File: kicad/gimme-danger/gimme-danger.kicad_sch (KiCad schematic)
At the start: 67 parts, among them J3 Screw_Terminal_01x06, Q1 AO3400A, Q2 AO3400A, Q3 AO3400A, Q4 AO3400A, U1 ESP32-S3-WROOM-1, U11 DDTC143EUA, U2 TYPE-C-31-M-12, U3 TPD4E1U06DCKR, U4 DC-84, U5 SKRKAEE020, U7 SKRKAEE020, U8 TPS54302, U9 INA219AIDR

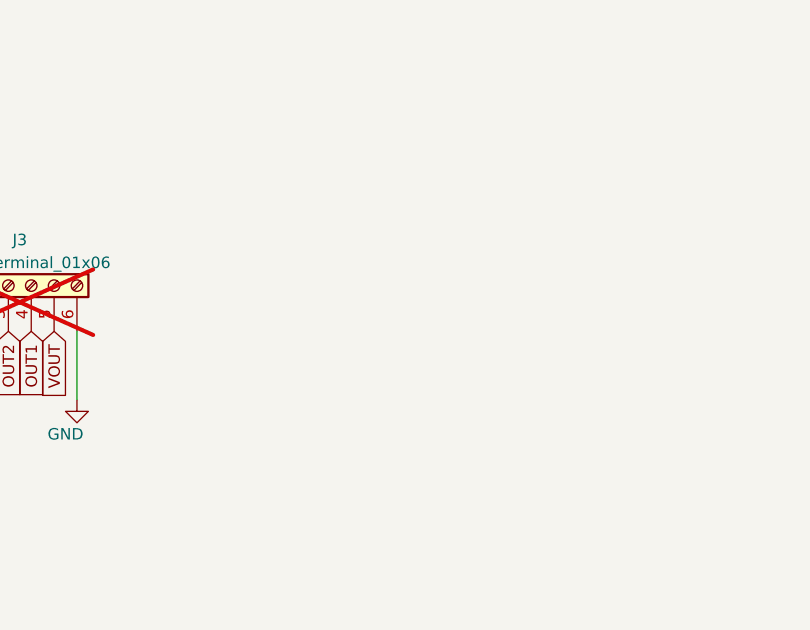
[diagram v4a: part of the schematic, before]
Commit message: Added mounting holes
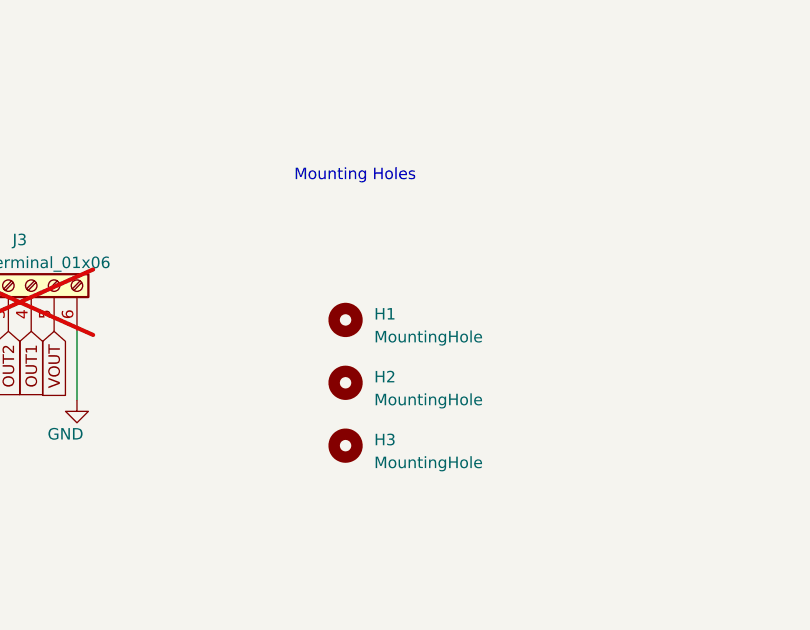
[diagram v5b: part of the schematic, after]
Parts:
- added H1, H2, H3: MountingHole, MountingHole:MountingHole_2.2mm_M2_Pad_Via, symbol Mechanical:MountingHole
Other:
- note added: "Mounting Holes"
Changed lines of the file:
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@@
+    (effects (font (size 1.27 1.27)) (justify left bottom))
+  )
+  (text "Mounting Holes" (at 119.38 220.345 0)
     (effects (font (size 1.27 1.27)) (justify left bottom))
   )
@@
     )
   )
+  (symbol (lib_id "Mechanical:MountingHole") (at 125.095 235.585 0) (unit 1)
+    (in_bom yes) (on_board yes) (dnp no) (fields_autoplaced)
+    (property "Reference" "H1" (at 128.27 234.95 0)
+      (effects (font (size 1.27 1.27)) (justify left))
+    )
+    (property "Value" "MountingHole" (at 128.27 237.49 0)
+      (effects (font (size 1.27 1.27)) (justify left))
+    )
+    (property "Footprint" "MountingHole:MountingHole_2.2mm_M2_Pad_Via" (at 125.095 235.585 0)
+      (effects (font (size 1.27 1.27)) hide)
+    )
+    (property "Datasheet" "~" (at 125.095 235.585 0)
+      (effects (font (size 1.27 1.27)) hide)
+    )
+    (instances
+      (project "gimme-danger"
+        (path "/1c42681d-64d0-4eab-a75f-10bf5c65177a"
+          (reference "H1") (unit 1)
+        )
+      )
+    )
+  )
   (symbol (lib_id "power:GND") (at 168.275 172.72 0) (unit 1)
     (in_bom yes) (on_board yes) (dnp no)
@@
     )
   )
+  (symbol (lib_id "Mechanical:MountingHole") (at 125.095 249.555 0) (unit 1)
+    (in_bom yes) (on_board yes) (dnp no) (fields_autoplaced)
+    (property "Reference" "H3" (at 128.27 248.92 0)
+      (effects (font (size 1.27 1.27)) (justify left))
+    )
+    (property "Value" "MountingHole" (at 128.27 251.46 0)
+      (effects (font (size 1.27 1.27)) (justify left))
+    )
+    (property "Footprint" "MountingHole:MountingHole_2.2mm_M2_Pad_Via" (at 125.095 249.555 0)
+      (effects (font (size 1.27 1.27)) hide)
+    )
+    (property "Datasheet" "~" (at 125.095 249.555 0)
+      (effects (font (size 1.27 1.27)) hide)
+    )
+    (instances
+      (project "gimme-danger"
+        (path "/1c42681d-64d0-4eab-a75f-10bf5c65177a"
+          (reference "H3") (unit 1)
+        )
+      )
+    )
+  )
   (symbol (lib_id "Device:C_Small") (at 272.288 146.685 0) (unit 1)
     (in_bom yes) (on_board yes) (dnp no)
@@
         )
       )
+    )
+  )
+  (symbol (lib_id "Mechanical:MountingHole") (at 125.095 242.57 0) (unit 1)
+    (in_bom yes) (on_board yes) (dnp no) (fields_autoplaced)
+    (property "Reference" "H2" (at 128.27 241.935 0)
+      (effects (font (size 1.27 1.27)) (justify left))
+    )
+    (property "Value" "MountingHole" (at 128.27 244.475 0)
+      (effects (font (size 1.27 1.27)) (justify left))
+    )
+    (property "Footprint" "MountingHole:MountingHole_2.2mm_M2_Pad_Via" (at 125.095 242.57 0)
+      (effects (font (size 1.27 1.27)) hide)
+    )
+    (property "Datasheet" "~" (at 125.095 242.57 0)
+      (effects (font (size 1.27 1.27)) hide)
+    )
+    (instances
+      (project "gimme-danger"
+        (path "/1c42681d-64d0-4eab-a75f-10bf5c65177a"
+          (reference "H2") (unit 1)
+        )
+      )

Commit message: v0.0.2a routing v0
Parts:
- removed H1, H2, H3: MountingHole, MountingHole:MountingHole_2.2mm_M2_Pad_Via, symbol Mechanical:MountingHole
- added C11: 220p, Capacitor_SMD:C_0402_1005Metric, symbol Device:C_Small
- added H1, H2, H3: MountingHole, MountingHole:MountingHole_2.2mm_M2_Pad_Via, symbol Mechanical:MountingHole_Pad
- added TP10, TP9: 3v3, TestPoint:TestPoint_Pad_D1.0mm, symbol Connector:TestPoint
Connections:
- net CC2: now also C11.1
- net GND: now also C11.2, H1.1, H2.1, H3.1, TP10.1, TP9.1

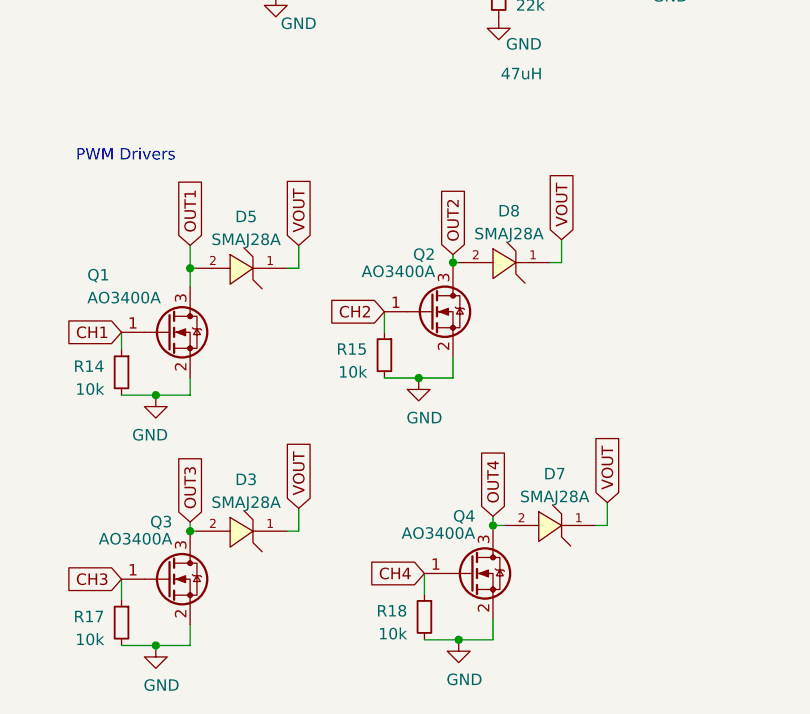
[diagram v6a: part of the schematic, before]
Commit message: Add schottky on ch1
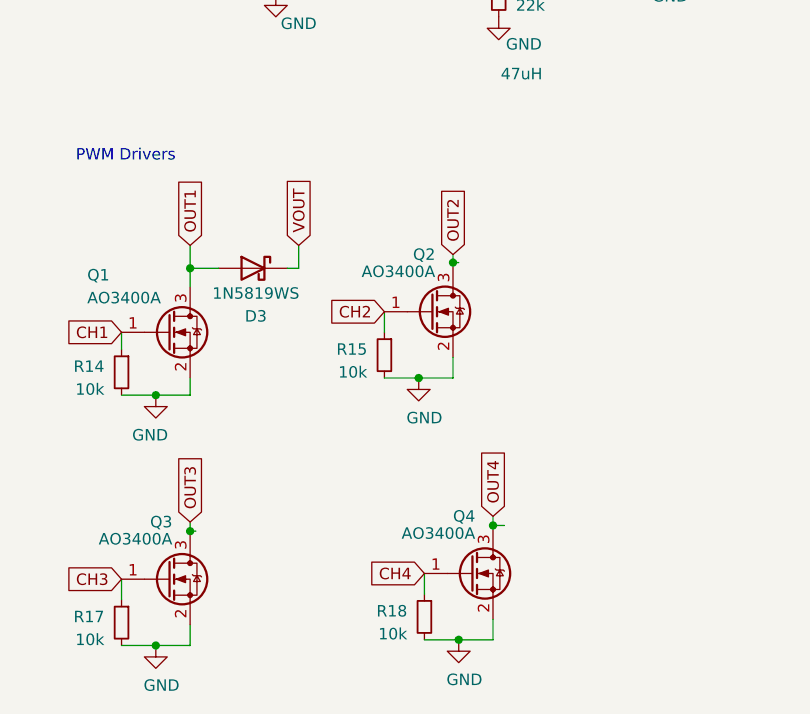
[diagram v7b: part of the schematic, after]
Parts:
- removed D3, D5, D7, D8: SMAJ28A, footprint:SMA_L4.3-W2.6-LS5.2-RD, symbol SMAJ28A_C283899:SMAJ28A_C283899
- added D3: 1N5819WS, Diode_SMD:D_SOD-323, symbol Diode:1N5819WS
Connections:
- net OUT1: now also D3.2 (A)
- net VOUT: now also D3.1 (K)

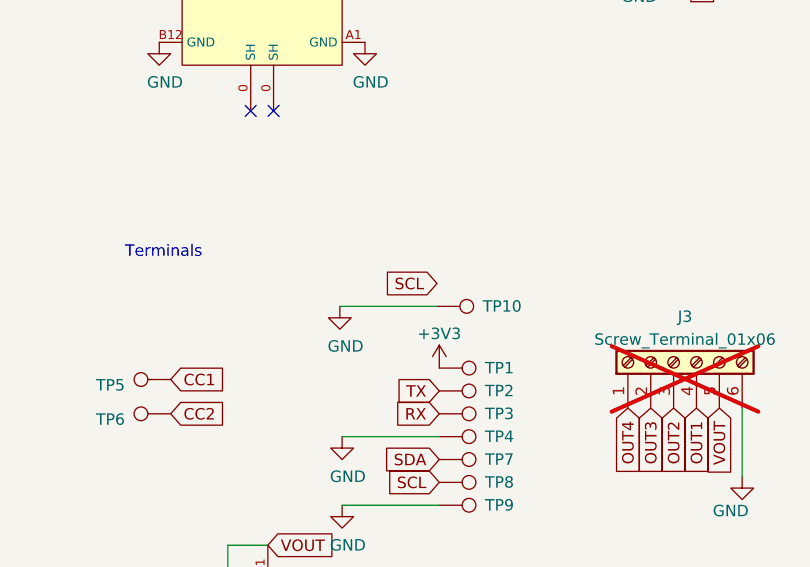
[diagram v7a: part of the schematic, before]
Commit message: No more DRC errors -- only 78 warnings
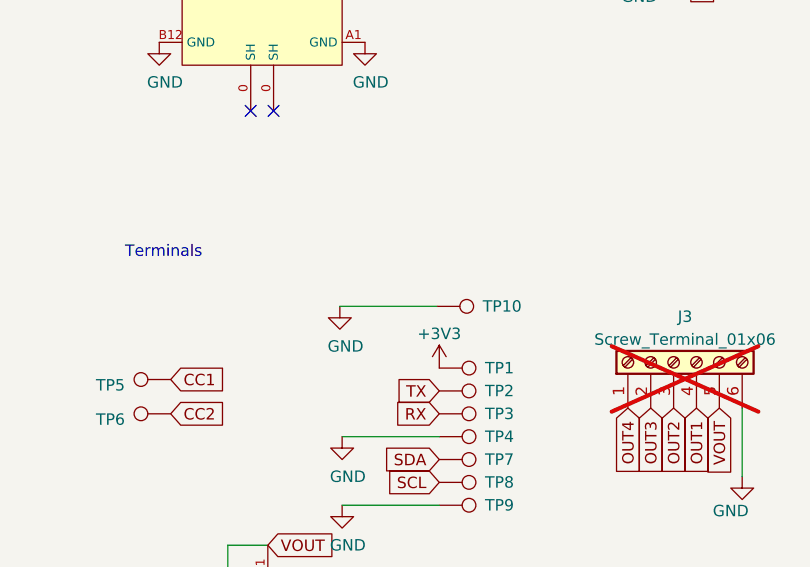
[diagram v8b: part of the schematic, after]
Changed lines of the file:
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@@
-    )
-  )
-  (global_label "SCL" (shape input) (at 61.341 223.012 180) (fields_autoplaced)
-    (effects (font (size 1.27 1.27)) (justify right))
-    (property "Intersheetrefs" "${INTERSHEET_REFS}" (at 54.9276 223.012 0)
-      (effects (font (size 1.27 1.27)) (justify right) hide)
     )
   )
